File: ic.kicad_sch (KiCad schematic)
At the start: 14 parts, among them U144 74LS148, U145 74HC04, U146 74HC138, U147 74HC02, U152 74HC02, U157 74HC02, U158 74HC02

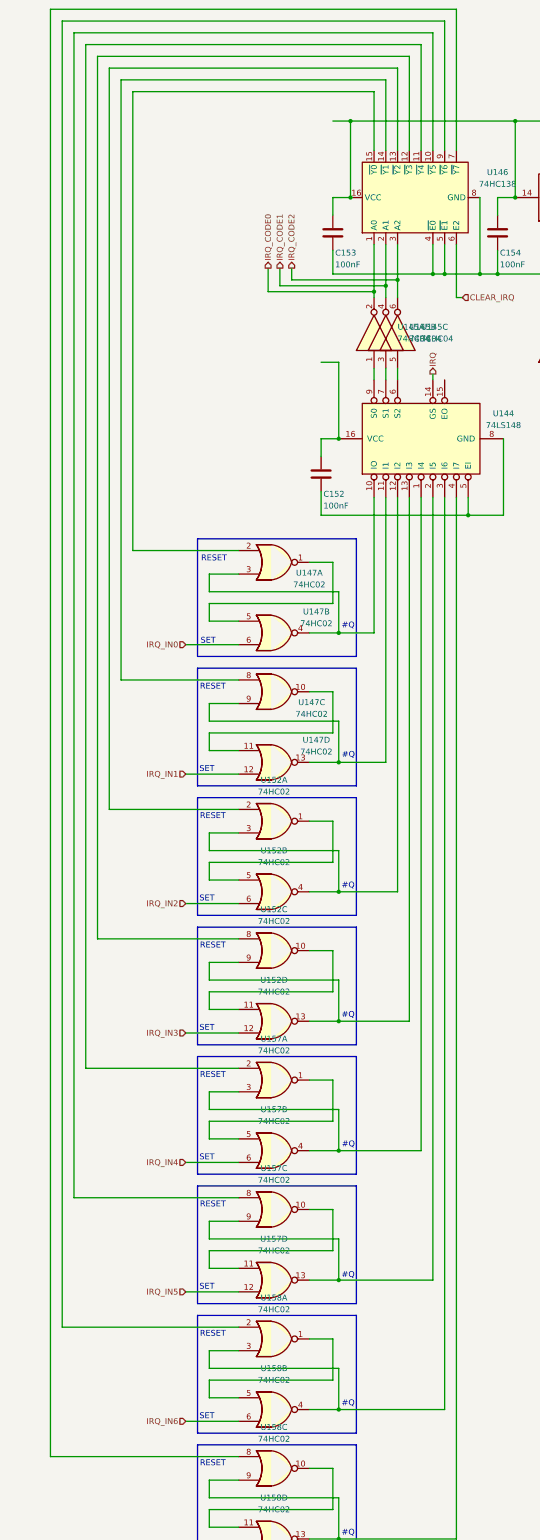
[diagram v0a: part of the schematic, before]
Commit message: feat: connected all control signals to cu
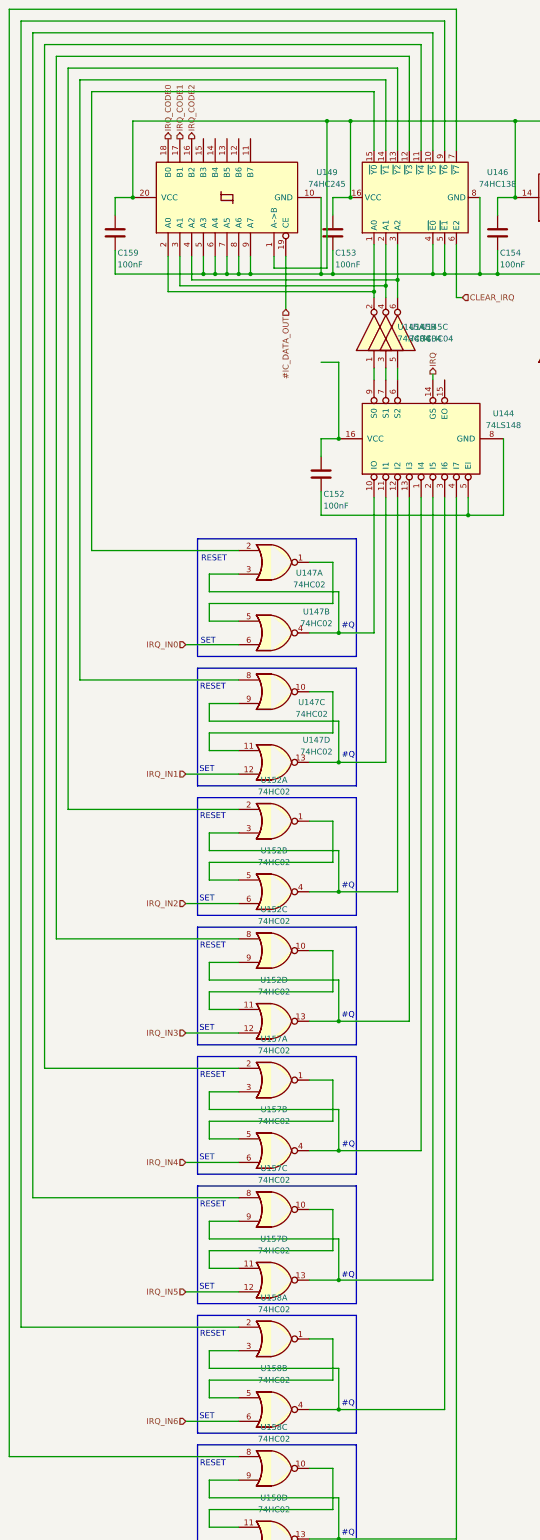
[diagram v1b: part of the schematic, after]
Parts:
- added C159: 100nF, Capacitor_THT:C_Disc_D3.0mm_W1.6mm_P2.50mm, symbol Device:C
- added U149: 74HC245, Connector_RJ:RJ45_HALO_HFJ11-x2450E-LxxRL_Horizontal, symbol 74xx:74HC245
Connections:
- net IRQ_CODE0: now also U149.18 (B0); no longer U145.2, U146.1 (A0)
- net IRQ_CODE1: now also U149.17 (B1); no longer U145.4, U146.2 (A1)
- net IRQ_CODE2: now also U149.16 (B2); no longer U145.6, U146.3 (A2)
- net at C153.1, C154.1, C155.1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: now also C159.1, U149.1 (A->B), U149.20 (VCC)
- net at C153.2, C154.2, C155.2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: now also C159.2, U149.10 (GND), U149.5 (A3), U149.6 (A4), U149.7 (A5), U149.8 (A6), U149.9 (A7)
- new net: U145.4, U146.2 (A1), U149.3 (A1)
- new net: U145.2, U146.1 (A0), U149.2 (A0)
- new net: U145.6, U146.3 (A2), U149.4 (A2)
- new net #IC_DATA_OUT: U149.19 (CE)
